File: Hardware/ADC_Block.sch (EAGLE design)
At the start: 34 parts, among them U1 ADS1015, U2 PCA9306, U3 3.3V

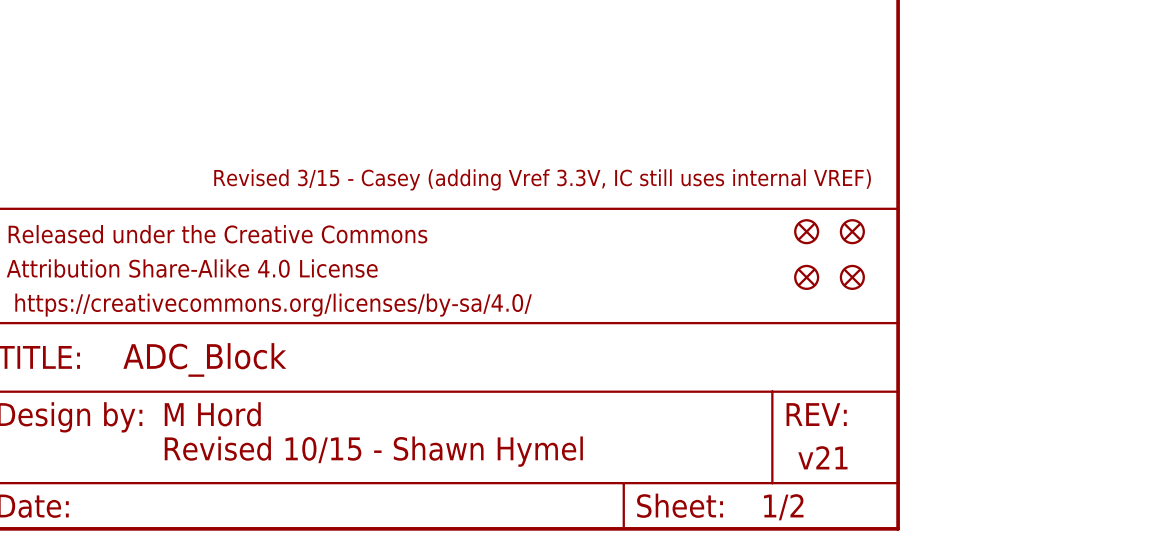
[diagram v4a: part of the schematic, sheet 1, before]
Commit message: Cleaned up traces. Moved revision notes on schematic.
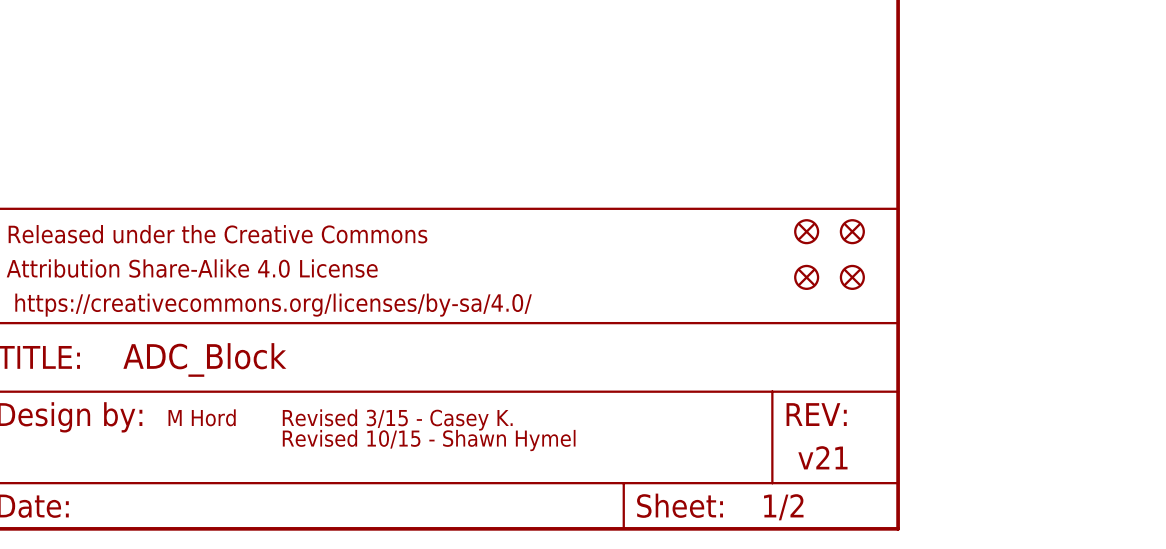
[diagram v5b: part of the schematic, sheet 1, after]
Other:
- note added: "Revised 3/15 - Casey K."
- note removed: "Revised 3/15 - Casey (adding Vref 3.3V, IC still uses internal VREF)"
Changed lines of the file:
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@@
 1001011 (0x4B)</text>
 <text x="237.744" y="6.604" size="2.54" layer="94">v21</text>
-<text x="167.132" y="11.43" size="2.54" layer="94">M Hord</text>
-<text x="172.72" y="38.1" size="1.778" layer="94">Revised 3/15 - Casey (adding Vref 3.3V, IC still uses internal VREF)</text>
+<text x="167.64" y="11.43" size="1.778" layer="94">M Hord</text>
+<text x="180.34" y="11.43" size="1.778" layer="94">Revised 3/15 - Casey K.</text>
 <text x="215.9" y="73.66" size="1.27" layer="91" rot="R180">Note: Bus Selection
 Default to I2C-1</text>
-<text x="167.132" y="7.62" size="2.54" layer="94">Revised 10/15 - Shawn Hymel</text>
+<text x="180.34" y="9.144" size="1.778" layer="94">Revised 10/15 - Shawn Hymel</text>
 </plain>
 <instances>

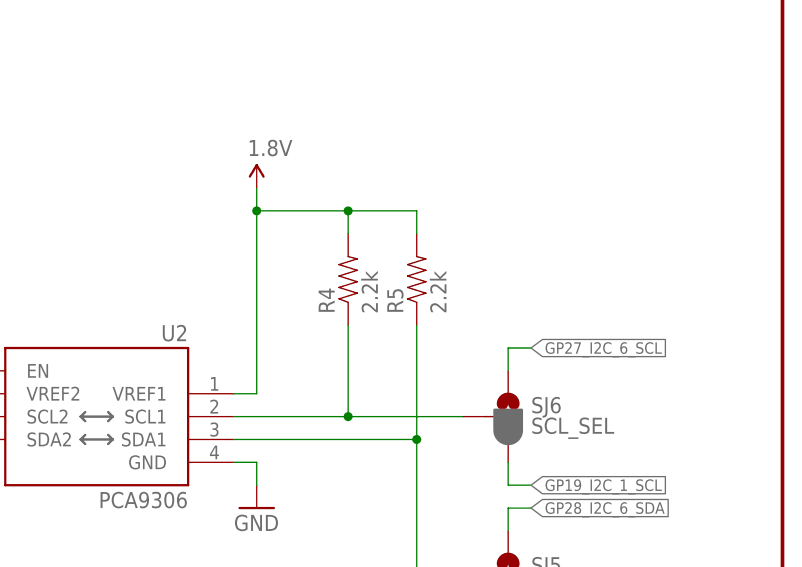
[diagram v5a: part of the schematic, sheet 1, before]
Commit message: Changed R4 and R5 to DNP, which is how they were in v21.
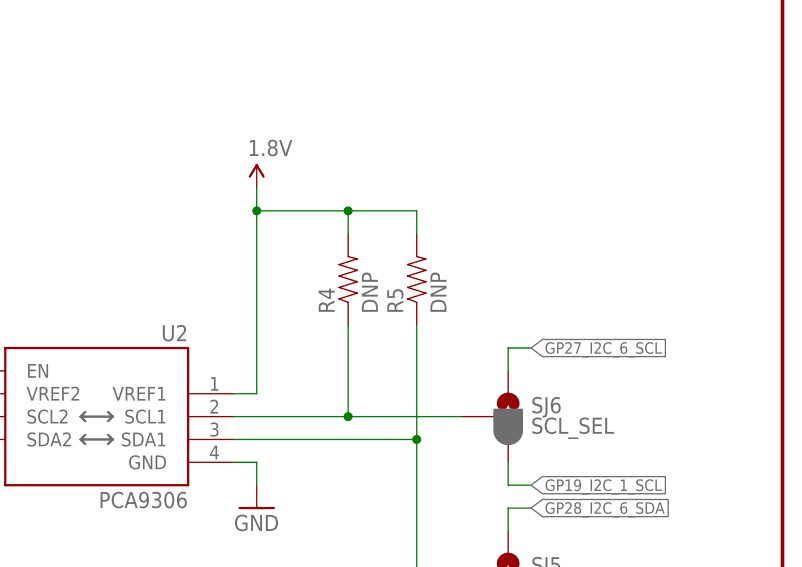
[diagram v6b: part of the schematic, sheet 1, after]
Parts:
- R4, R5: value 2.2k -> DNP
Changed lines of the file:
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@@
 <setting verticaltext="up"/>
 </settings>
-<grid distance="0.1" unitdist="inch" unit="inch" style="lines" multiple="1" display="yes" altdistance="0.01" altunitdist="inch" altunit="inch"/>
+<grid distance="0.1" unitdist="inch" unit="inch" style="lines" multiple="1" display="no" altdistance="0.01" altunitdist="inch" altunit="inch"/>
 <layers>
 <layer number="1" name="Top" color="4" fill="1" visible="no" active="no"/>
@@
 <part name="SUPPLY4" library="SparkFun-Aesthetics" deviceset="1.8V" device=""/>
 <part name="R3" library="SparkFun-Resistors" deviceset="200KOHM1/10W1%(0603)" device="200K" value="200k"/>
-<part name="R4" library="SparkFun-Resistors" deviceset="2.2KOHM-1/10W-1%(0603)" device="" value="2.2k"/>
-<part name="R5" library="SparkFun-Resistors" deviceset="2.2KOHM-1/10W-1%(0603)" device="" value="2.2k"/>
+<part name="R4" library="SparkFun-Resistors" deviceset="2.2KOHM-1/10W-1%(0603)" device="" value="DNP"/>
+<part name="R5" library="SparkFun-Resistors" deviceset="2.2KOHM-1/10W-1%(0603)" device="" value="DNP"/>
 <part name="GND2" library="SparkFun-Aesthetics" deviceset="GND" device=""/>
 <part name="GND5" library="SparkFun-Aesthetics" deviceset="GND" device=""/>

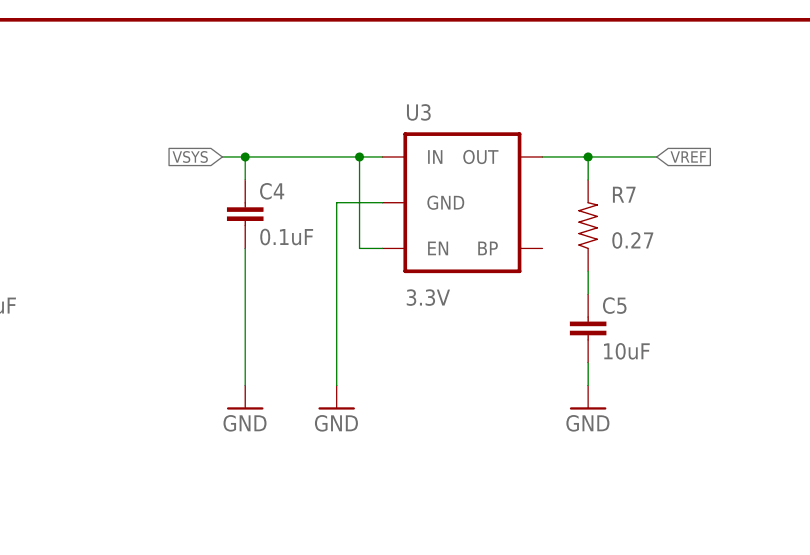
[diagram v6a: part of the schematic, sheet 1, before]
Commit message: Moved pin 1 markers to outside packages on IC and Hirose connectors.
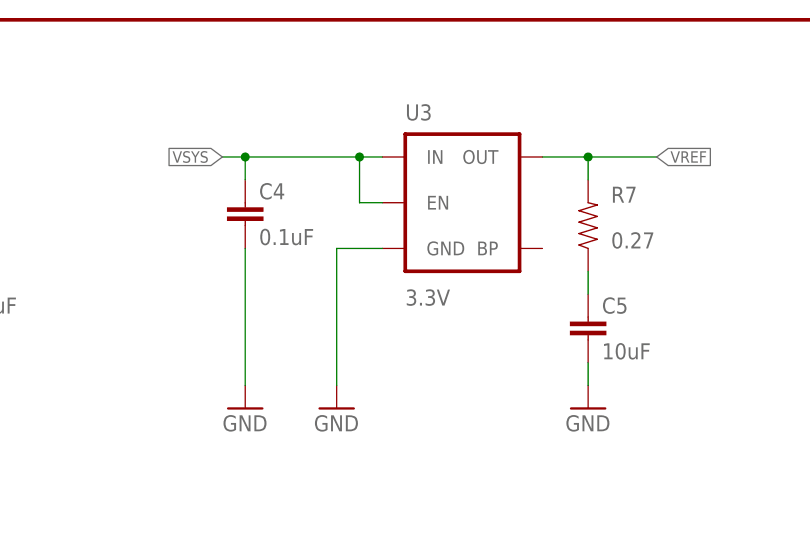
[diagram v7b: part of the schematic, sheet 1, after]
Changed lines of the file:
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@@
 <pinref part="U3" gate="G$1" pin="GND"/>
 <pinref part="GND9" gate="1" pin="GND"/>
-<wire x1="88.9" y1="165.1" x2="83.82" y2="165.1" width="0.1524" layer="91"/>
-<wire x1="83.82" y1="165.1" x2="83.82" y2="144.78" width="0.1524" layer="91"/>
+<wire x1="88.9" y1="160.02" x2="83.82" y2="160.02" width="0.1524" layer="91"/>
+<wire x1="83.82" y1="160.02" x2="83.82" y2="144.78" width="0.1524" layer="91"/>
 </segment>
 <segment>
@@
 <segment>
 <pinref part="U3" gate="G$1" pin="EN"/>
-<wire x1="88.9" y1="160.02" x2="86.36" y2="160.02" width="0.1524" layer="91"/>
-<wire x1="86.36" y1="160.02" x2="86.36" y2="170.18" width="0.1524" layer="91"/>
+<wire x1="88.9" y1="165.1" x2="86.36" y2="165.1" width="0.1524" layer="91"/>
+<wire x1="86.36" y1="165.1" x2="86.36" y2="170.18" width="0.1524" layer="91"/>
 <pinref part="U3" gate="G$1" pin="IN"/>
 <wire x1="86.36" y1="170.18" x2="88.9" y2="170.18" width="0.1524" layer="91"/>

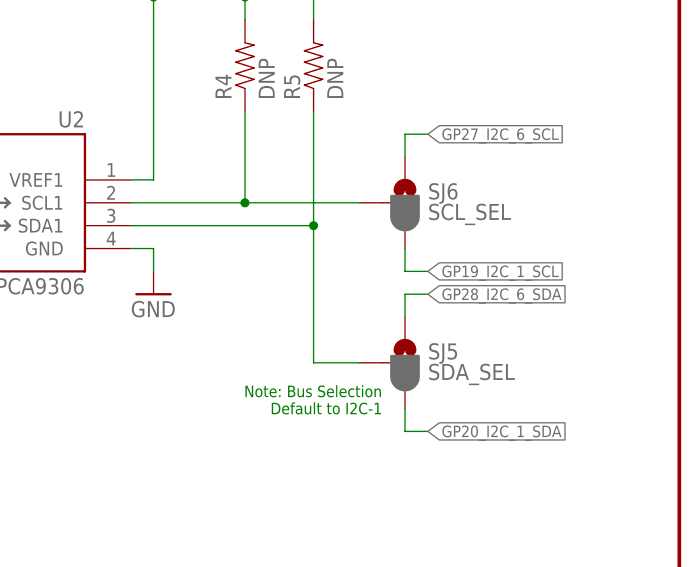
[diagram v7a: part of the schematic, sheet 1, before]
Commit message: Changed solder jumper to make I2C_6 default
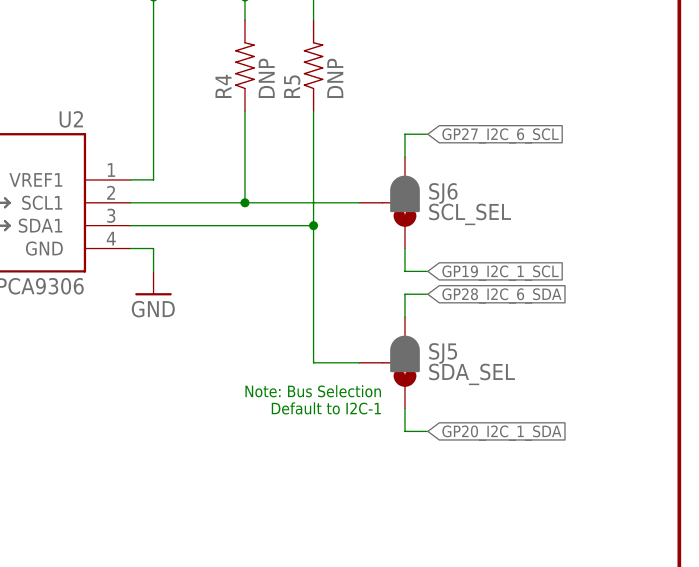
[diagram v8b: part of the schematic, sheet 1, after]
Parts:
- SJ5, SJ6: device SparkFun-Passives:JUMPER-PAD-3-2OF3_NC_BY_PASTE -> SparkFun-Passives:JUMPER_PAD-3-1&2_NC_BY_PASTE
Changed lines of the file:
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@@
 <?xml version="1.0" encoding="utf-8"?>
 <!DOCTYPE eagle SYSTEM "eagle.dtd">
-<eagle version="7.2.0">
+<eagle version="7.3.0">
 <drawing>
 <settings>
@@
 <part name="GND9" library="SparkFun-Aesthetics" deviceset="GND" device=""/>
 <part name="GND10" library="SparkFun-Aesthetics" deviceset="GND" device=""/>
-<part name="SJ5" library="SparkFun-Passives" deviceset="JUMPER-PAD-3-2OF3_NC_BY_PASTE" device="" value="SDA_SEL"/>
-<part name="SJ6" library="SparkFun-Passives" deviceset="JUMPER-PAD-3-2OF3_NC_BY_PASTE" device="" value="SCL_SEL"/>
+<part name="SJ5" library="SparkFun-Passives" deviceset="JUMPER_PAD-3-1&amp;2_NC_BY_PASTE" device="" value="SDA_SEL"/>
+<part name="SJ6" library="SparkFun-Passives" deviceset="JUMPER_PAD-3-1&amp;2_NC_BY_PASTE" device="" value="SCL_SEL"/>
 <part name="R7" library="SparkFun-Resistors" deviceset="0.27OHM-1/10W-1%(0603)" device="" value="0.27"/>
 </parts>
